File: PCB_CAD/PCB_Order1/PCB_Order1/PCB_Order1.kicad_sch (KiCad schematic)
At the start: 2 parts, among them IC1 TC58BVG1S3HTA00, U1 STM32H7A3ZITx

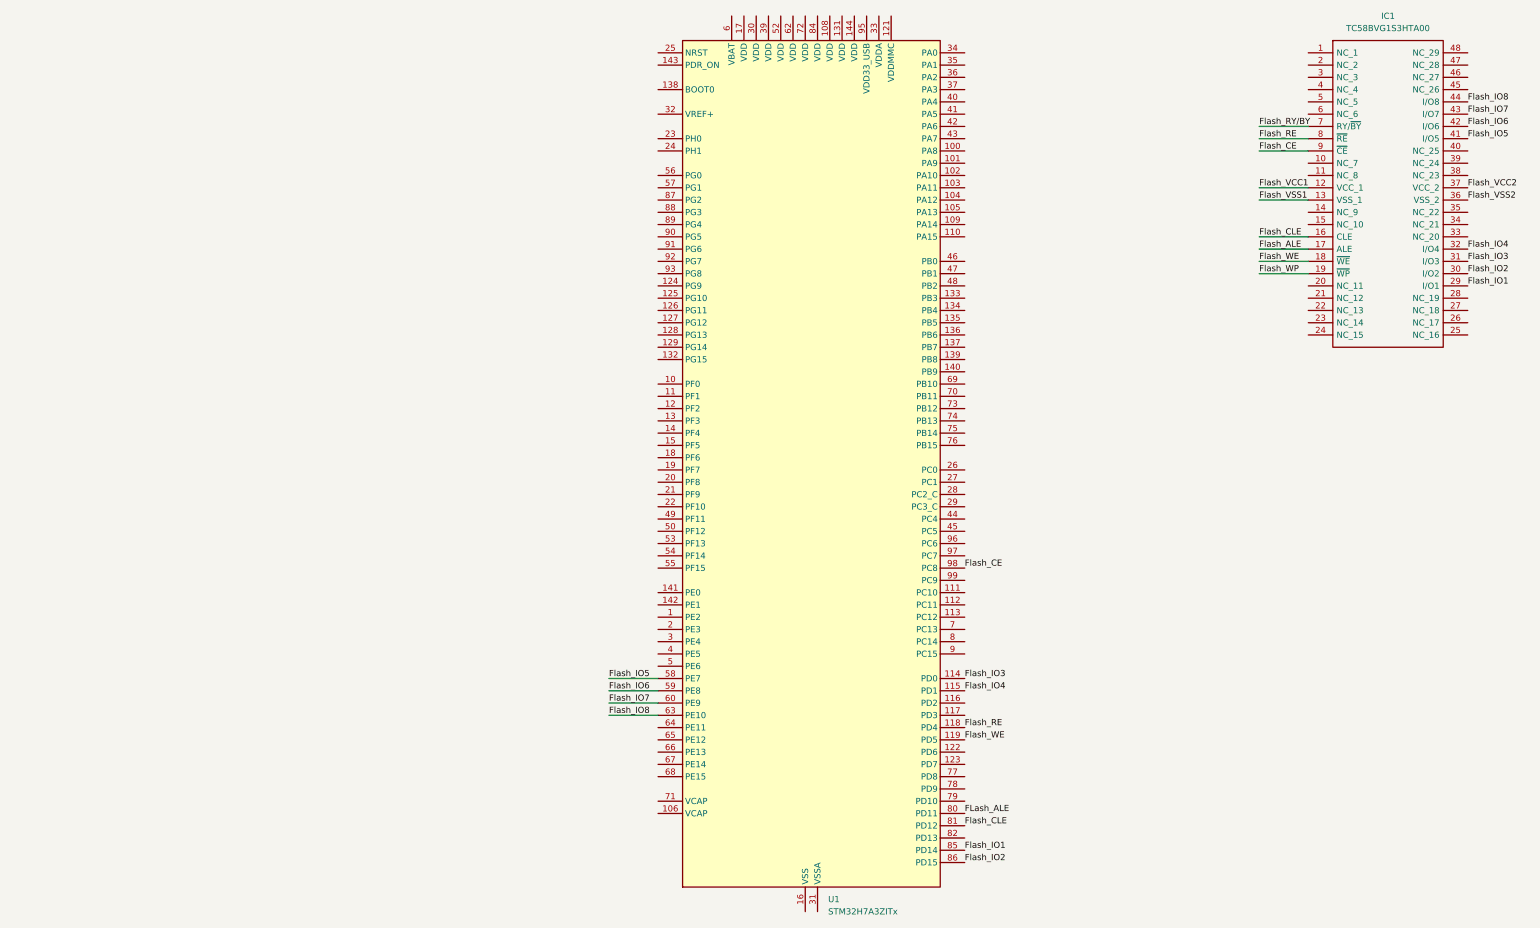
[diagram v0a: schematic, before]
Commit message: added my adc pinouts to main circuit schematic in kicad
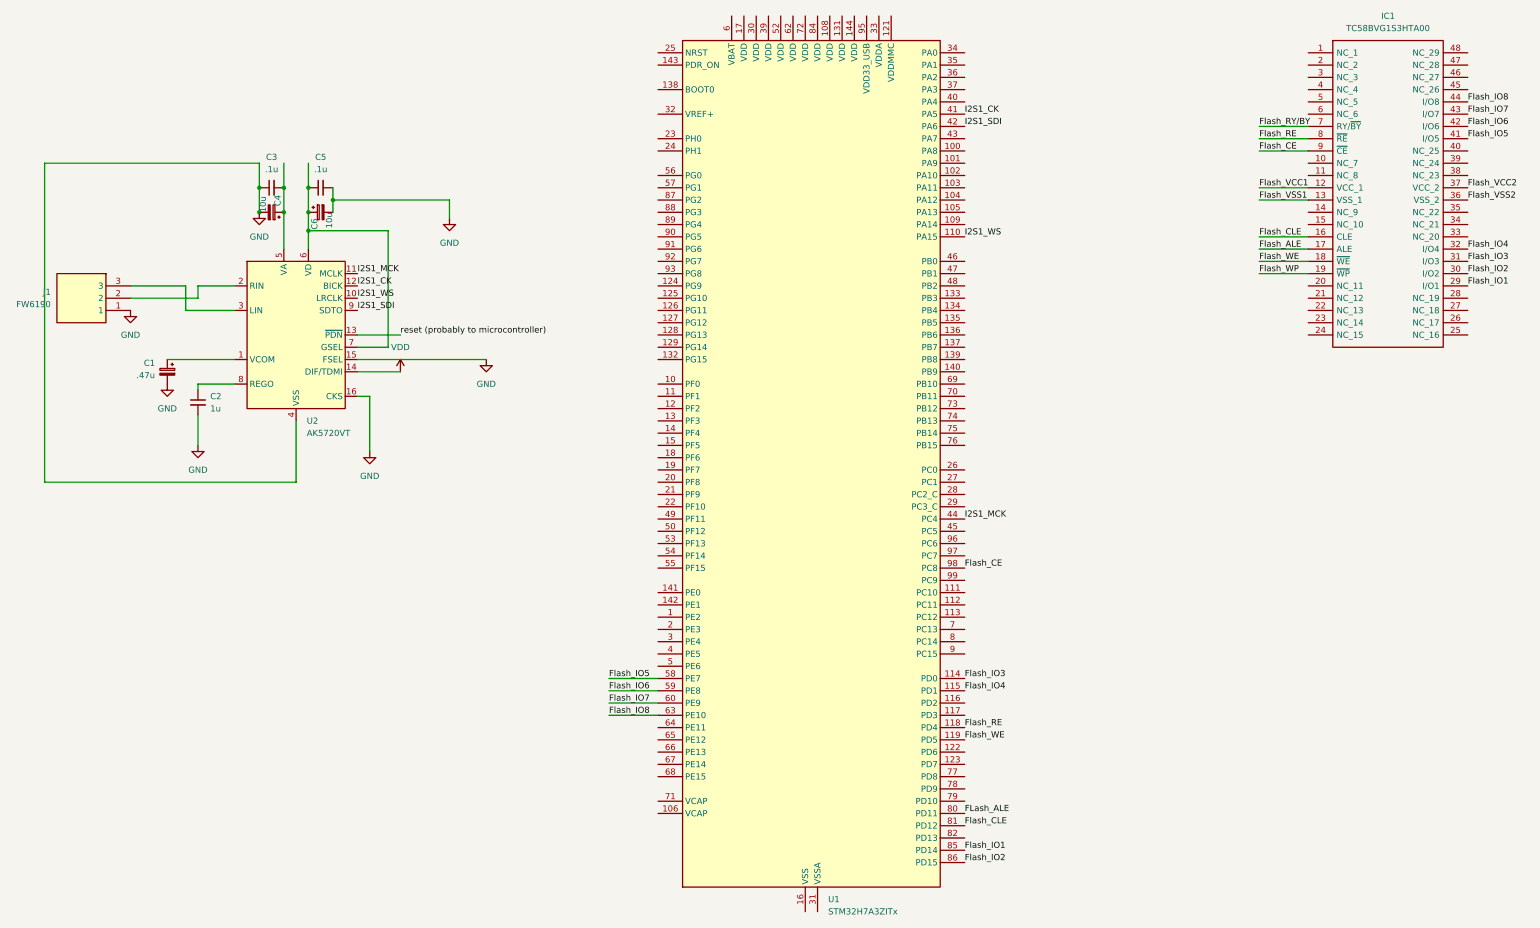
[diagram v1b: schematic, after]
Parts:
- added C1: .47u, Capacitor_SMD:C_0805_2012Metric, symbol Device:C_Polarized_Small
- added C2: 1u, Capacitor_SMD:C_0805_2012Metric, symbol Device:C_Small
- added C3, C5: .1u, Capacitor_SMD:C_0805_2012Metric, symbol Device:C_Small
- added C4, C6: 10u, Capacitor_SMD:C_0805_2012Metric, symbol Device:C_Polarized_Small
- added J1: FW6190, CustomModels:FW6190, symbol FW6190:FW6190
- added U2: AK5720VT, Package_SO:TSSOP-16_4.4x5mm_P0.65mm, symbol Audio:AK5720VT
- IC1: footprint SOP50P2000X120-48N -> KiCad:SOP50P2000X120-48N
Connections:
- net I2S1_WS: now reaches U1.110 (PA15)
- net I2S1_WS: now also U2.10 (LRCLK)
- net I2S1_CK: now reaches U1.41 (PA5)
- net I2S1_CK: now also U2.12 (BICK)
- net I2S1_SDI: now reaches U1.42 (PA6)
- net I2S1_SDI: now also U2.9 (SDTO)
- net I2S1_MCK: now reaches U1.44 (PC4)
- net I2S1_MCK: now also U2.11 (MCLK)
- new net: J1.2, U2.2 (RIN)
- new net: J1.3, U2.3 (LIN)
- new net: C3.2, C4.1, U2.5 (VA)
- new net: C2.1, U2.8 (REGO)
- new net: C5.1, C6.1, U2.6 (VD), U2.7 (GSEL)
- new net: C1.1, U2.1 (VCOM)
- new net GND: C1.2, C2.2, C3.1, C4.2, C5.2, C6.2, J1.1, U2.15 (FSEL), U2.16 (CKS), U2.4 (VSS)
- new net VDD: U2.14 (DIF/TDMI)
- new net reset (probably to microcontroller): U2.13 (~{PDN})
